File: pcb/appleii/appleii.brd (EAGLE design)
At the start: 75 x 45 mm, 28 parts, among them J1 ATX24RH

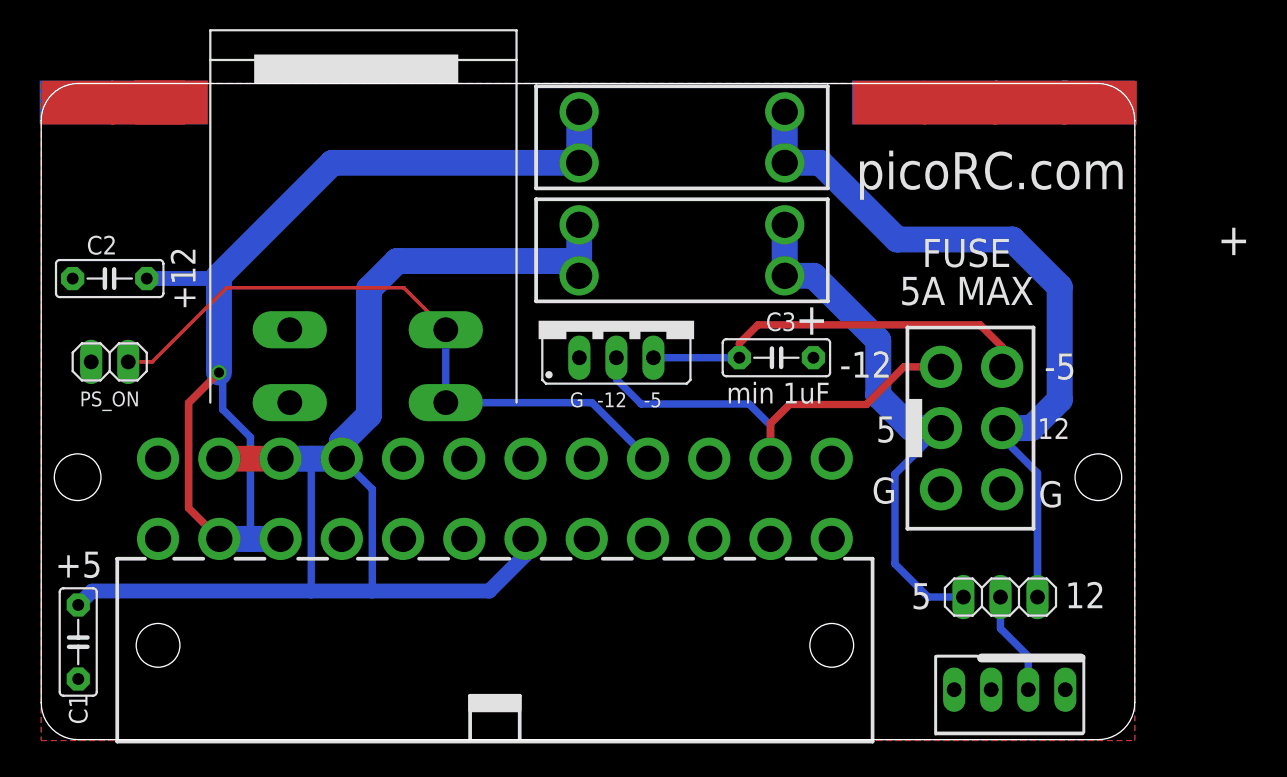
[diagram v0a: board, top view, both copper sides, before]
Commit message: added more caps
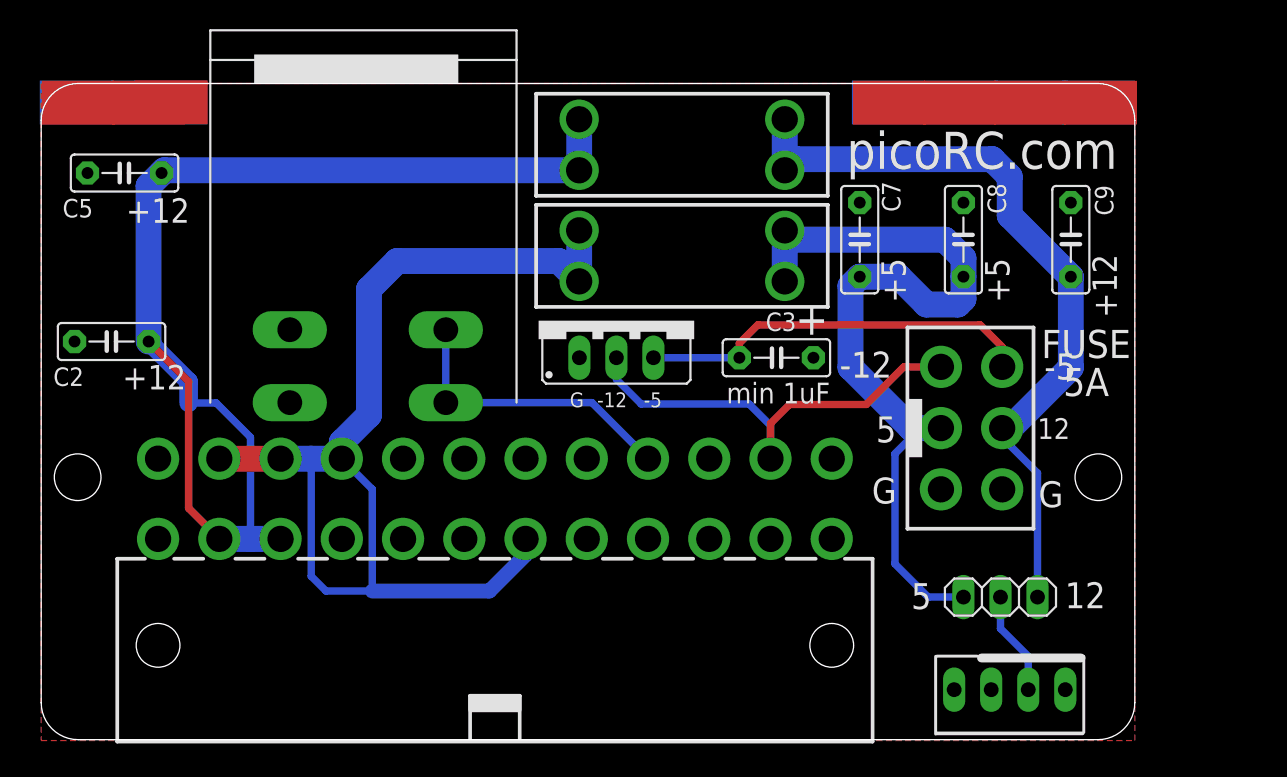
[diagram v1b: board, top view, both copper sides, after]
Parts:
- removed C1: (no value), capacitor-wima:C5B2.5
- removed JP1: (no value), pinhead:1X02
- added C5, C7, C8, C9: (no value), capacitor-wima:C5B2.5
- moved C2 4.32 mm to (4.83, 27.3)
- moved U$2 0.51 mm to (43.9, 40.8)
- moved U$1 0.38 mm to (43.9, 33.2)
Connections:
- net +12V: now also C9.1
- net +5V: now also C7.1, C8.1
- net GND: now also C5.2, C7.2, C8.2, C9.2; no longer C1.2, JP1.2
- net N$5: no longer JP1.1
- net N$6: no longer C1.1
- net N$8: now also C5.1
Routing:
- net N$5: track 45.5 -> 20.5 mm
- net +5V: track 37.0 -> 58.6 mm
- net N$6: track 92.1 -> 75.3 mm
- net N$8: track 85.8 -> 91.6 mm, vias 1 -> 0
- net +12V: track 51.0 -> 53.6 mm
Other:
- board text added: "FUSE 5A"
- board text added: "dekuNukem 2023"
- board text removed: "FUSE 5A MAX"
- board text removed: "PD2 dekuNukem APR23"
- board text removed: "PS_ON"

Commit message: changed to 70L05
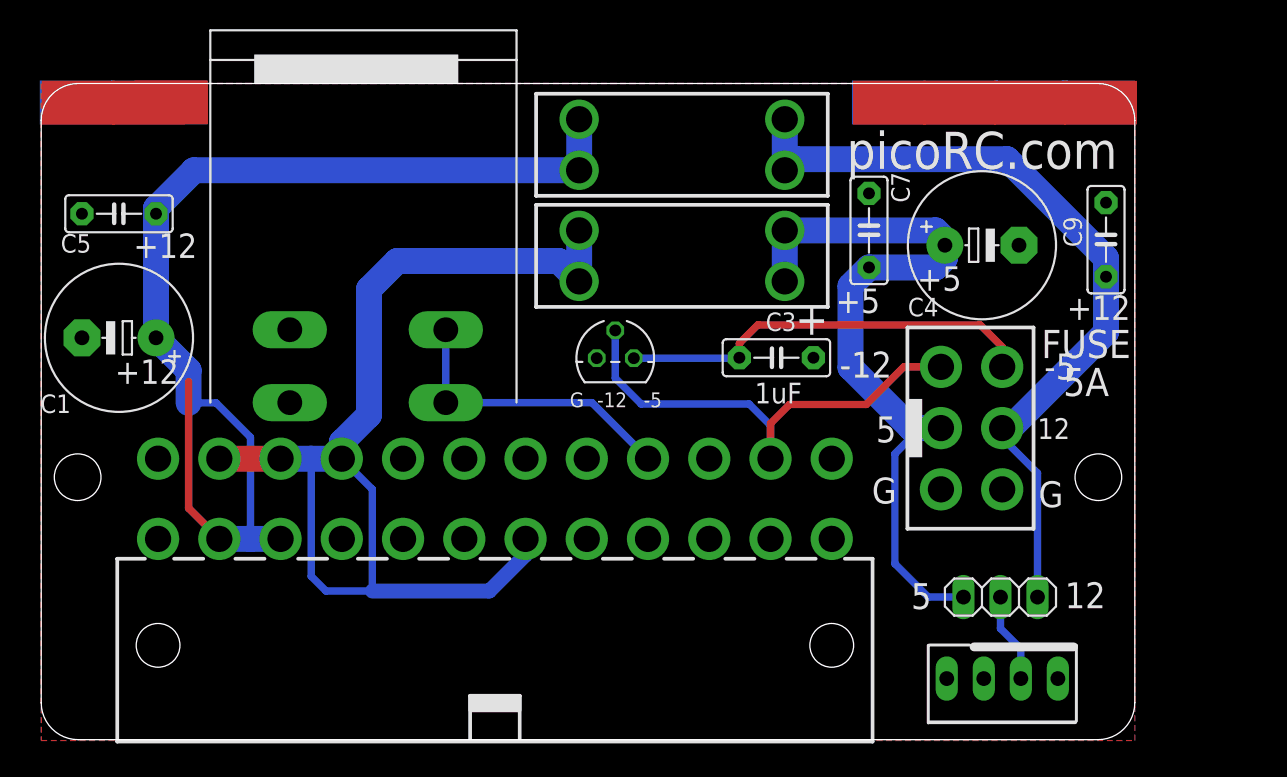
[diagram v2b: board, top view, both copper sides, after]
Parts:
- removed C2, C8: (no value), capacitor-wima:C5B2.5
- removed IC1: (no value), v-reg:79XXS
- added C1, C4: (no value), adafruit:E5-10,5
- added IC2: (no value), linear:TO92
- moved C5 2.82 mm to (5.33, 36.1)
- moved C9 2.41 mm to (73.0, 34.3)
- moved JP3 0.92 mm to (65.9, 4.19)
- moved C7 0.90 mm to (56.8, 34.9)
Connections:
- net +5V: now also C4.+; no longer C8.1
- net -12V: now also IC2.2; no longer IC1.IN
- net -5V: now also IC2.3; no longer IC1.OUT
- net GND: now also C1.-, C4.-, IC2.1; no longer C2.2, C8.2, IC1.GND
- net N$8: now also C1.+; no longer C2.1
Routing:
- net N$8: track 91.6 -> 86.1 mm
- net +5V: track 58.6 -> 53.9 mm
- net +12V: track 53.6 -> 56.2 mm
- net -12V: track 31.4 -> 33.3 mm
- net -5V: track 27.4 -> 28.8 mm
- net N$1: track 7.14 -> 6.17 mm
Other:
- board text added: "1uF"
- board text removed: "min 1uF"

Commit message: switched back to 7905
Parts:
- removed IC2: (no value), linear:TO92
- added IC1: (no value), v-reg:79XXS
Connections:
- net -12V: now also IC1.IN; no longer IC2.2
- net -5V: now also IC1.OUT; no longer IC2.3
- net GND: now also IC1.GND; no longer IC2.1
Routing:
- net -12V: track 33.3 -> 31.1 mm
- net -5V: track 28.8 -> 27.6 mm
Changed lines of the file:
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@@
 <attribute name="VALUE" x="75.819" y="32.258" size="1.27" layer="27" ratio="10" rot="R90"/>
-</element>
-<element name="IC2" library="linear" library_urn="urn:adsk.eagle:library:262" package="TO92" package3d_urn="urn:adsk.eagle:package:16416/2" value="" x="39.37" y="26.162" smashed="yes">
-<attribute name="POPULARITY" value="0" x="39.37" y="26.162" size="1.778" layer="27" display="off"/>
-<attribute name="VALUE" x="42.291" y="24.892" size="1.27" layer="27" ratio="10"/>
 </element>
 <element name="C1" library="adafruit" package="E5-10,5" value="" x="5.334" y="27.559" smashed="yes" rot="R180">
@@
 <attribute name="POPULARITY" value="10" x="5.334" y="36.068" size="1.778" layer="27" rot="R180" display="off"/>
 <attribute name="VALUE" x="7.366" y="38.862" size="1.27" layer="27" ratio="10" rot="R180"/>
+</element>
+<element name="IC1" library="v-reg" library_urn="urn:adsk.eagle:library:409" package="79XXS" package3d_urn="urn:adsk.eagle:package:30343/1" value="" x="39.37" y="28.448" smashed="yes">
+<attribute name="POPULARITY" value="3" x="39.37" y="29.464" size="1.778" layer="27" display="off"/>
+<attribute name="VALUE" x="34.29" y="20.828" size="1.27" layer="27" ratio="10"/>
 </element>
 </elements>
@@
 <contactref element="C7" pad="2"/>
 <contactref element="C9" pad="2"/>
-<contactref element="IC2" pad="1"/>
 <contactref element="C1" pad="-"/>
 <contactref element="C4" pad="-"/>
 <contactref element="C5" pad="2"/>
+<contactref element="IC1" pad="GND"/>
 <wire x1="72.644" y1="43.688" x2="72.5" y2="43.7" width="0" layer="19" extent="1-16"/>
 <wire x1="8.9" y1="43.7" x2="8.928" y2="43.706" width="0" layer="19" extent="1-16"/>
@@
 <wire x1="59.164" y1="25.568" x2="61.704" y2="25.568" width="0.508" layer="1"/>
 <wire x1="51.32" y1="22.987" x2="56.583" y2="22.987" width="0.508" layer="1"/>
-<contactref element="IC2" pad="2"/>
-<wire x1="41.148" y1="23.019" x2="39.37" y2="24.797" width="0.508" layer="16"/>
-<wire x1="39.37" y1="24.797" x2="39.37" y2="28.067" width="0.508" layer="16"/>
+<wire x1="39.37" y1="24.797" x2="41.148" y2="23.019" width="0.508" layer="16"/>
+<contactref element="IC1" pad="IN"/>
+<wire x1="39.37" y1="25.908" x2="39.37" y2="24.797" width="0.508" layer="16"/>
 </signal>
 <signal name="N$6">
@@
 <contactref element="U$3" pad="P$2"/>
 <contactref element="U$3" pad="P$4"/>
-<wire x1="41.615" y1="19.269" x2="37.77" y2="23.114" width="0.508" layer="16"/>
-<wire x1="37.77" y1="23.114" x2="27.748" y2="23.114" width="0.508" layer="16"/>
+<wire x1="41.615" y1="19.269" x2="38.278" y2="22.606" width="0.508" layer="16"/>
+<wire x1="38.278" y1="22.606" x2="28.256" y2="22.606" width="0.508" layer="16"/>
+<wire x1="28.256" y1="22.606" x2="27.748" y2="23.114" width="0.508" layer="16"/>
 <wire x1="27.748" y1="28.114" x2="27.748" y2="23.114" width="0.508" layer="16"/>
 </signal>
@@
 <wire x1="65.904" y1="26.933" x2="65.904" y2="25.568" width="0.508" layer="1"/>
 <wire x1="64.389" y1="28.448" x2="65.904" y2="26.933" width="0.508" layer="1"/>
-<contactref element="IC2" pad="3"/>
-<wire x1="40.64" y1="26.162" x2="47.847" y2="26.162" width="0.508" layer="16"/>
-<wire x1="47.847" y1="26.162" x2="47.879" y2="26.194" width="0.508" layer="16"/>
+<contactref element="IC1" pad="OUT"/>
+<wire x1="41.91" y1="25.908" x2="42.196" y2="26.194" width="0.508" layer="16"/>
+<wire x1="42.196" y1="26.194" x2="47.879" y2="26.194" width="0.508" layer="16"/>
 </signal>
 <signal name="N$1">

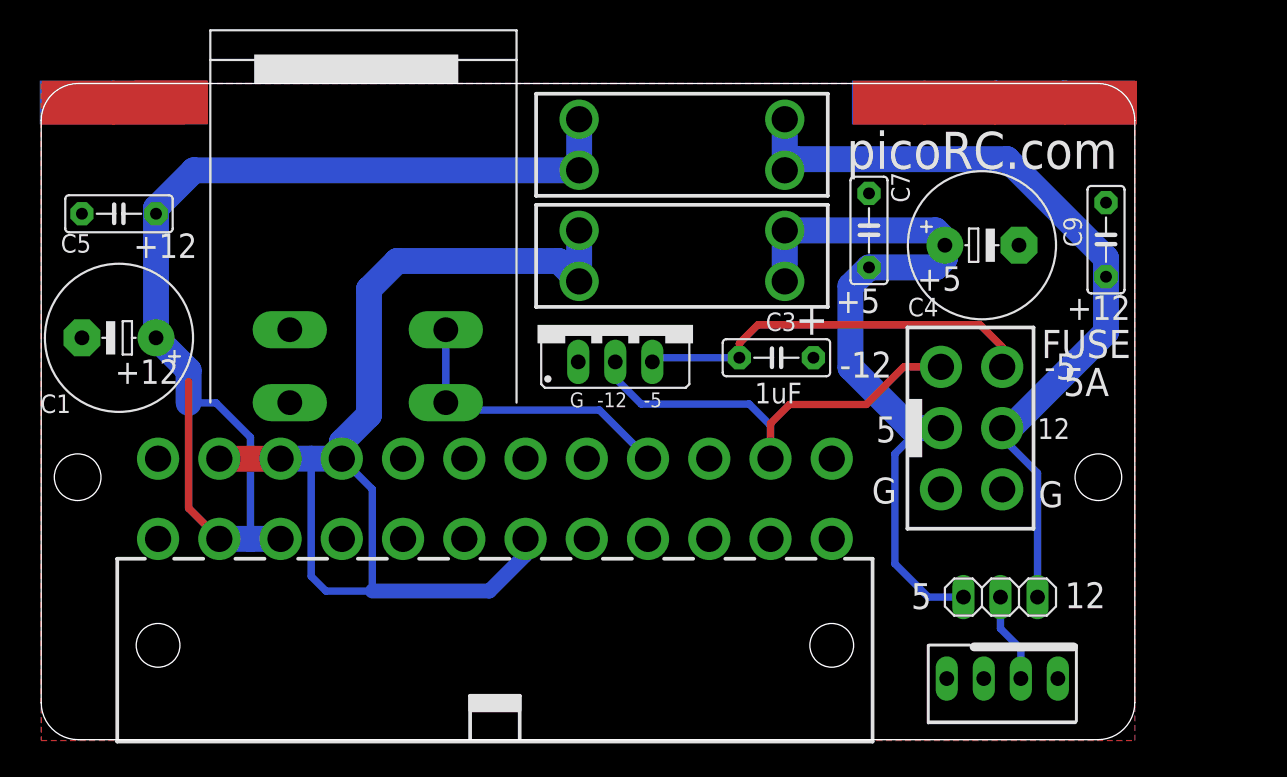
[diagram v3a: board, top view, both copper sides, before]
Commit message: added more caps
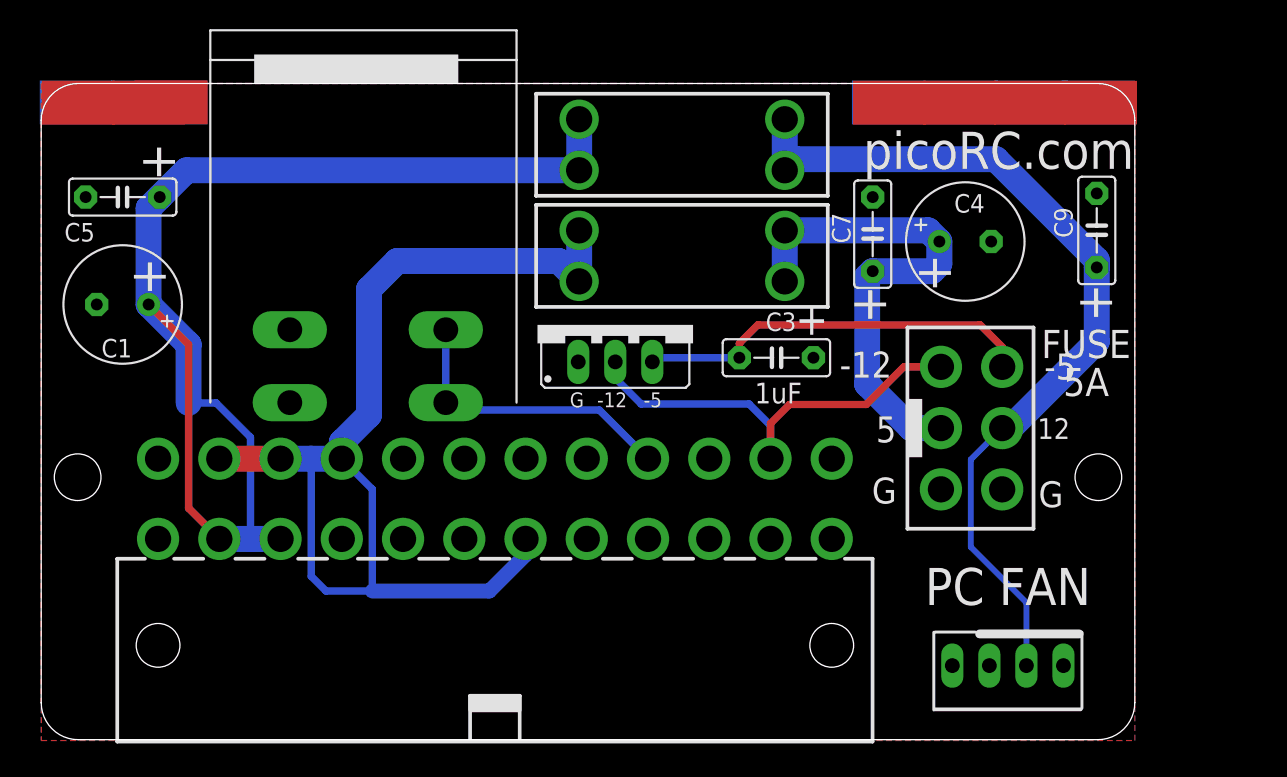
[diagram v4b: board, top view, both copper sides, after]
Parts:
- removed JP2: (no value), pinhead:1X03
- C1, C4: device adafruit:E5-10,5 -> adafruit_changed:E3,5-8
- moved C1 2.30 mm to (5.59, 29.8)
- moved C4 1.17 mm to (63.4, 34.2)
- moved C5 1.17 mm to (5.59, 37.2)
- moved JP3 0.97 mm to (66.3, 5.08)
- moved C9 0.90 mm to (72.4, 34.9)
- moved C7 0.36 mm to (57.0, 34.7)
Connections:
- removed net N$1: JP2.2, JP3.2
- net +12V: now also JP3.2; no longer JP2.3
- net +5V: no longer JP2.1
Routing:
- net +5V: track 53.9 -> 34.9 mm
- net N$8: track 86.1 -> 93.3 mm
- net N$1: track 6.17 -> 0.00 mm
- net +12V: track 56.2 -> 61.4 mm
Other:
- board text added: "PC FAN"
- board text removed: "+12"
- board text removed: "+5"

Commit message: cleanup for new run
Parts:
- added C2: (no value), capacitor-wima:C5B2.5
- moved C5 64.9 mm to (70.5, 34.9), turned to 270 degrees
- moved JP3 1.92 mm to (66.0, 6.99)
- moved C4 1.42 mm to (64.6, 34.8)
- moved C7 1.17 mm to (55.9, 34.9)
- moved C9 1.15 mm to (73.5, 35.1)
- moved U$20 0.40 mm to (72.4, 44.1)
- moved U$17 0.38 mm to (58.1, 44.1)
- moved U$18 0.38 mm to (63.1, 44.1)
- moved U$19 0.38 mm to (67.9, 44.1)
- moved C1 0.25 mm to (5.59, 29.6)
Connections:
- net +12V: now also C5.1
- net +5V: now also C2.1
- net GND: now also C2.2
- net N$8: no longer C5.1
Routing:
- net +5V: track 34.9 -> 39.2 mm
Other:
- board text added: "USE 5A FUSE"
- board text removed: "FUSE 5A"
